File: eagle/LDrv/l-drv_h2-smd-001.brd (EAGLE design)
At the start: 100 x 80 mm, 34 parts, among them IC2 74AC132D, IC3 74AC132D, IC4 74AC132D

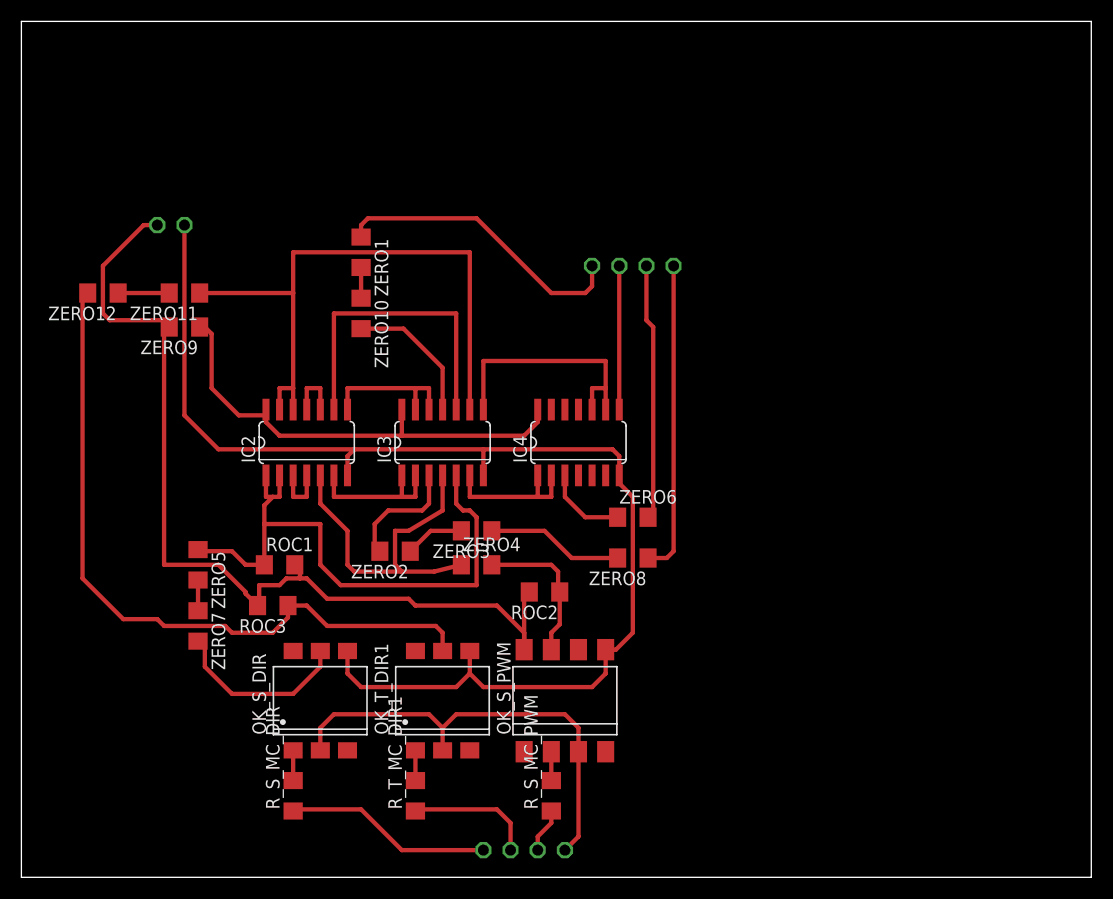
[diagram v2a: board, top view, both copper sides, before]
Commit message: SMD for logic drv
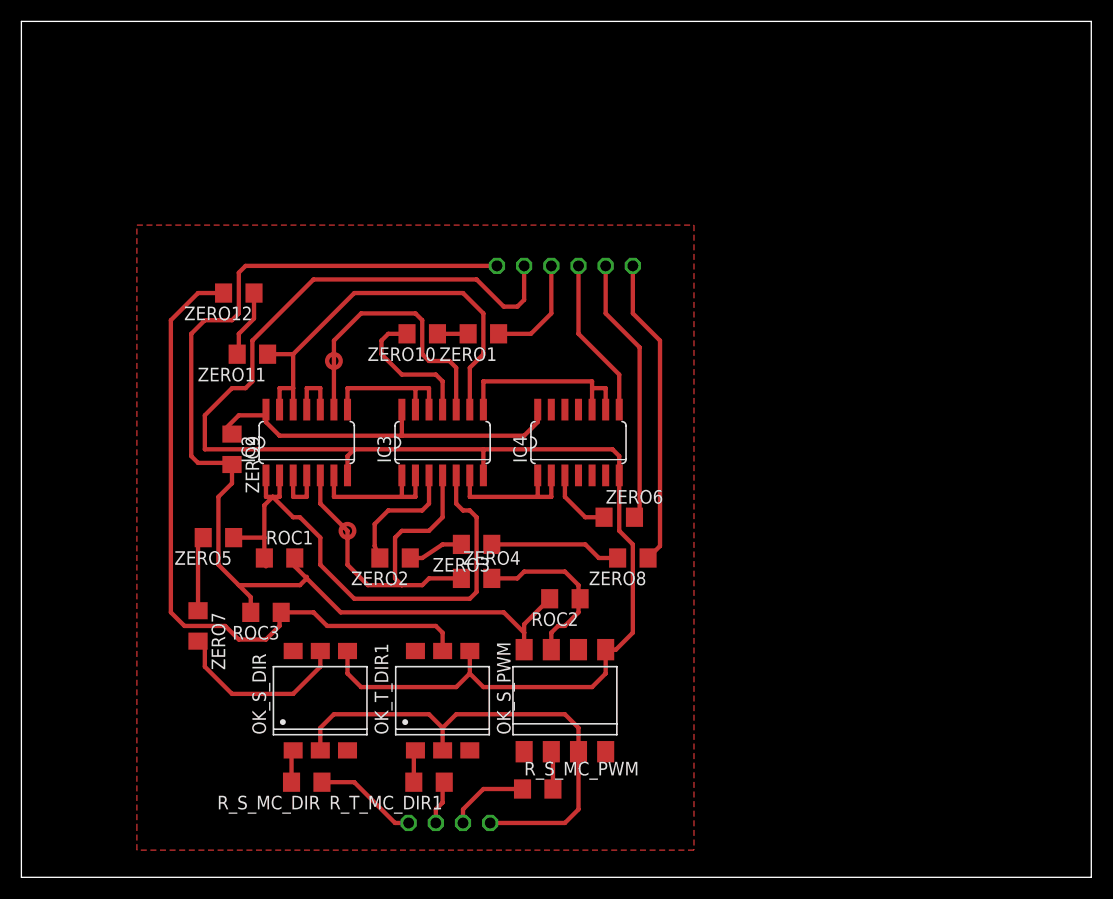
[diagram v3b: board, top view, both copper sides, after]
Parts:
- moved JP6_VCC 32.0 mm to (44.5, 57.1)
- moved JP9_GND 32.0 mm to (47.0, 57.1)
- moved ZERO1 13.7 mm to (43.2, 50.8), turned to 180 degrees
- moved ZERO12 12.7 mm to (20.3, 54.6)
- moved ZERO9 12.3 mm to (19.7, 40.0), turned to 270 degrees
- moved ZERO11 8.54 mm to (21.6, 48.9)
- moved JP10 7.43 mm to (41.3, 5.08)
- moved JP11 7.43 mm to (43.8, 5.08)
- moved JP12 7.43 mm to (38.7, 5.08)
- moved JP5 7.43 mm to (36.2, 5.08)
- moved ZERO10 6.02 mm to (37.5, 50.8), turned to 180 degrees
- moved JP_H1 3.81 mm to (57.1, 57.1)
- moved JP_H2 3.81 mm to (49.5, 57.1)
- moved JP_L1 3.81 mm to (54.6, 57.1)
- moved JP_L2 3.81 mm to (52.1, 57.1)
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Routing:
- net GND: track 118.0 -> 142.0 mm
- net N$13: track 28.0 -> 10.2 mm
- net N$D2: track 57.9 -> 41.3 mm
- net N$26: track 88.4 -> 101.9 mm
- net N$6: track 19.4 -> 9.68 mm
- net N$8: track 12.0 -> 4.14 mm
- net VCC: track 43.8 -> 36.4 mm
- net N$21: track 23.8 -> 18.7 mm
- net MC_GND: track 42.4 -> 46.8 mm
- net N$22: track 2.87 -> 7.03 mm
- net N$D1: track 55.3 -> 51.8 mm
- net N$7: track 4.18 -> 7.62 mm
- net N$27: track 67.1 -> 63.9 mm
- net N$20: track 14.1 -> 16.5 mm
- net N$28: track 4.78 -> 6.37 mm
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- added copper zone on layer 1, net N$29
